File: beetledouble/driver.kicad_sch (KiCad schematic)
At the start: 13 parts, among them J4 motor_out, Q1 IRF8313PBF, Q2 IRF8313PBF, U4 NCP81155MNTXG, U5 NCP81155MNTXG

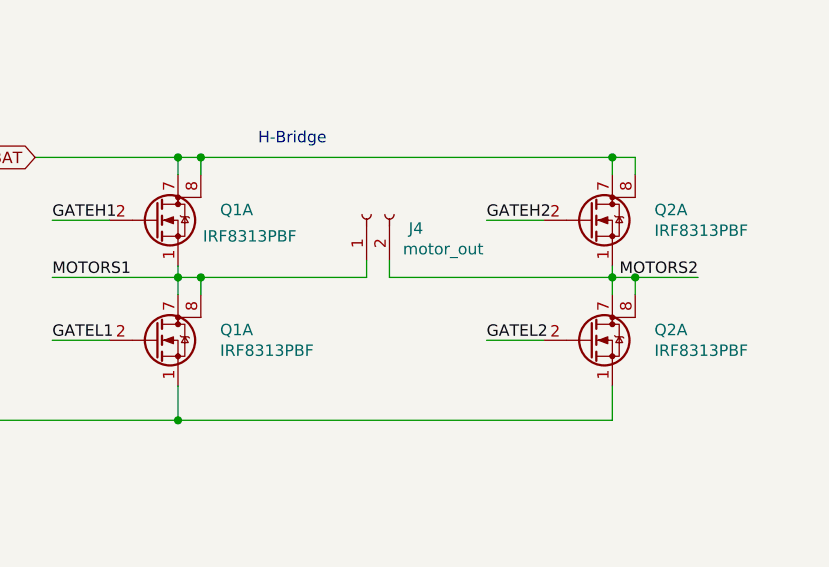
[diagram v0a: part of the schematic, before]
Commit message: Beetle double driver update with differen fets
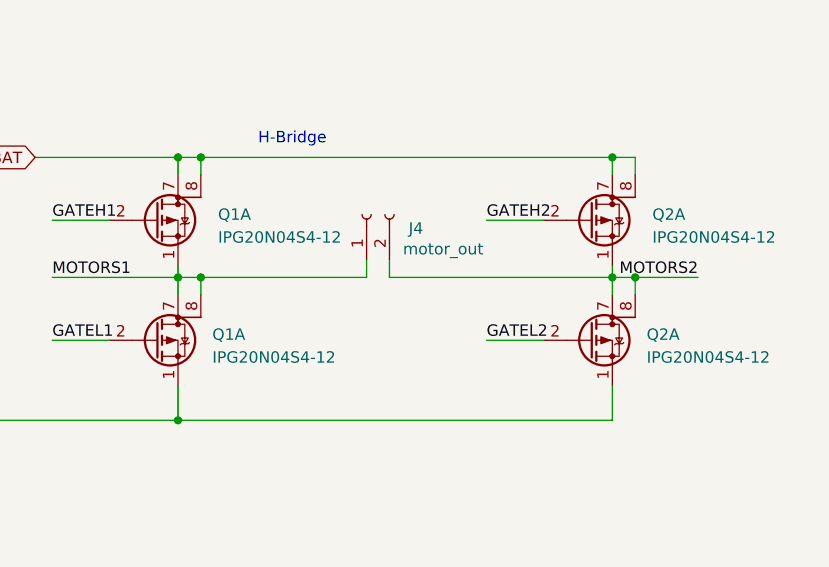
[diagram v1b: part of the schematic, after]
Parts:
- removed Q1 (x2), Q2 (x2): IRF8313PBF, Package_SO:SOIC-8_3.9x4.9mm_P1.27mm, symbol beetletriple:Q_Dual_NMOS_S1G1S2G2D2D2D1D1
- added Q1 (x2), Q2 (x2): IPG20N04S4-12, beetledouble:Infineon-PG-TDSON, symbol Device:Q_Dual_PMOS_S1G1S2G2D2D2D1D1
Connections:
- net GATEH2: now also Q2.2 (G)
- net GATEL2: now also Q2.2 (G)
- net GNDSHUNT: now also Q1.1 (S), Q2.1 (S)
- net MOTORS1: now also Q1.1 (S), Q1.7 (D), Q1.8 (G)
- net MOTORS2: now also Q2.1 (S), Q2.7 (D), Q2.8 (G)
- net TESTH1: now also Q1.2 (G)
- net TESTL1: now also Q1.2 (G)
- net VBAT: now also Q1.7 (D), Q1.8 (G), Q2.7 (D), Q2.8 (G)
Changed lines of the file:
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@@
     (pin "2")
   )
-  (symbol (lib_id "beetletriple:Q_Dual_NMOS_S1G1S2G2D2D2D1D1") (at 201.295 78.74 0)
-    (in_bom yes) (on_board yes)
-    (property "Reference" "Q1" (id 0) (at 208.5087 77.5906 0)
+  (symbol (lib_id "Device:Q_Dual_PMOS_S1G1S2G2D2D2D1D1") (at 201.295 78.74 0)
+    (in_bom yes) (on_board yes) (fields_autoplaced)
+    (property "Reference" "Q1" (id 0) (at 208.28 78.1049 0)
       (effects (font (size 1.27 1.27)) (justify left))
     )
-    (property "Value" "IRF8313PBF " (id 1) (at 206.604 80.524 0)
+    (property "Value" "IPG20N04S4-12" (id 1) (at 208.28 80.6449 0)
       (effects (font (size 1.27 1.27)) (justify left))
     )
-    (property "Footprint" "Package_SO:SOIC-8_3.9x4.9mm_P1.27mm" (id 2) (at 206.375 78.74 0)
+    (property "Footprint" "beetledouble:Infineon-PG-TDSON" (id 2) (at 202.565 78.74 0)
       (effects (font (size 1.27 1.27)) hide)
     )
-    (property "Datasheet" "~" (id 3) (at 206.375 78.74 0)
-      (effects (font (size 1.27 1.27)) hide)
-    )
-    (property "LCSC" "C57696" (id 4) (at 201.295 78.74 0)
+    (property "Datasheet" "~" (id 3) (at 202.565 78.74 0)
       (effects (font (size 1.27 1.27)) hide)
     )
@@
     (pin "8")
   )
-  (symbol (lib_id "beetletriple:Q_Dual_NMOS_S1G1S2G2D2D2D1D1") (at 201.295 92.075 0)
-    (in_bom yes) (on_board yes)
-    (property "Reference" "Q1" (id 0) (at 208.5087 90.9256 0)
+  (symbol (lib_id "Device:Q_Dual_PMOS_S1G1S2G2D2D2D1D1") (at 201.295 92.075 0)
+    (in_bom yes) (on_board yes) (fields_autoplaced)
+    (property "Reference" "Q1" (id 0) (at 207.645 91.4399 0)
       (effects (font (size 1.27 1.27)) (justify left))
     )
-    (property "Value" "IRF8313PBF " (id 1) (at 208.509 93.224 0)
+    (property "Value" "IPG20N04S4-12" (id 1) (at 207.645 93.9799 0)
       (effects (font (size 1.27 1.27)) (justify left))
     )
-    (property "Footprint" "Package_SO:SOIC-8_3.9x4.9mm_P1.27mm" (id 2) (at 206.375 92.075 0)
+    (property "Footprint" "beetledouble:Infineon-PG-TDSON" (id 2) (at 202.565 92.075 0)
       (effects (font (size 1.27 1.27)) hide)
     )
-    (property "Datasheet" "~" (id 3) (at 206.375 92.075 0)
-      (effects (font (size 1.27 1.27)) hide)
-    )
-    (property "LCSC" "C57696" (id 4) (at 201.295 92.075 0)
+    (property "Datasheet" "~" (id 3) (at 202.565 92.075 0)
       (effects (font (size 1.27 1.27)) hide)
     )
@@
     (pin "6")
   )
-  (symbol (lib_id "beetletriple:Q_Dual_NMOS_S1G1S2G2D2D2D1D1") (at 249.555 78.74 0)
-    (in_bom yes) (on_board yes)
-    (property "Reference" "Q2" (id 0) (at 256.7687 77.5906 0)
+  (symbol (lib_id "Device:Q_Dual_PMOS_S1G1S2G2D2D2D1D1") (at 249.555 78.74 0)
+    (in_bom yes) (on_board yes) (fields_autoplaced)
+    (property "Reference" "Q2" (id 0) (at 256.54 78.1049 0)
       (effects (font (size 1.27 1.27)) (justify left))
     )
-    (property "Value" "IRF8313PBF " (id 1) (at 256.769 79.889 0)
+    (property "Value" "IPG20N04S4-12" (id 1) (at 256.54 80.6449 0)
       (effects (font (size 1.27 1.27)) (justify left))
     )
-    (property "Footprint" "Package_SO:SOIC-8_3.9x4.9mm_P1.27mm" (id 2) (at 254.635 78.74 0)
+    (property "Footprint" "beetledouble:Infineon-PG-TDSON" (id 2) (at 250.825 78.74 0)
       (effects (font (size 1.27 1.27)) hide)
     )
-    (property "Datasheet" "~" (id 3) (at 254.635 78.74 0)
-      (effects (font (size 1.27 1.27)) hide)
-    )
-    (property "LCSC" "C57696" (id 4) (at 249.555 78.74 0)
+    (property "Datasheet" "~" (id 3) (at 250.825 78.74 0)
       (effects (font (size 1.27 1.27)) hide)
     )
@@
     (pin "8")
   )
-  (symbol (lib_id "beetletriple:Q_Dual_NMOS_S1G1S2G2D2D2D1D1") (at 249.555 92.075 0)
-    (in_bom yes) (on_board yes)
-    (property "Reference" "Q2" (id 0) (at 256.7687 90.9256 0)
+  (symbol (lib_id "Device:Q_Dual_PMOS_S1G1S2G2D2D2D1D1") (at 249.555 92.075 0)
+    (in_bom yes) (on_board yes) (fields_autoplaced)
+    (property "Reference" "Q2" (id 0) (at 255.905 91.4399 0)
       (effects (font (size 1.27 1.27)) (justify left))
     )
-    (property "Value" "IRF8313PBF " (id 1) (at 256.769 93.224 0)
+    (property "Value" "IPG20N04S4-12" (id 1) (at 255.905 93.9799 0)
       (effects (font (size 1.27 1.27)) (justify left))
     )
-    (property "Footprint" "Package_SO:SOIC-8_3.9x4.9mm_P1.27mm" (id 2) (at 254.635 92.075 0)
+    (property "Footprint" "beetledouble:Infineon-PG-TDSON" (id 2) (at 250.825 92.075 0)
       (effects (font (size 1.27 1.27)) hide)
     )
-    (property "Datasheet" "~" (id 3) (at 254.635 92.075 0)
+    (property "Datasheet" "~" (id 3) (at 250.825 92.075 0)
       (effects (font (size 1.27 1.27)) hide)
     )
-    (property "LCSC" "C57696" (id 4) (at 249.555 92.075 0)
-      (effects (font (size 1.27 1.27)) hide)
-    )

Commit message: beetledouble esc wip
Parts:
- renumbered C3 to C5, C4 to C6, J4 to J5, Q1 to Q3, Q2 to Q4, R1 to R5, R2 to R6, R3 to R7, R4 to R8, U4 to U6, U5 to U7
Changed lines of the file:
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@@
   (symbol (lib_id "power:+12V") (at 48.26 91.44 0)
     (in_bom yes) (on_board yes)
-    (property "Reference" "#PWR06" (id 0) (at 48.26 95.25 0)
+    (property "Reference" "#PWR010" (id 0) (at 48.26 95.25 0)
       (effects (font (size 1.27 1.27)) hide)
     )
@@
   (symbol (lib_id "power:+12V") (at 48.895 40.64 0)
     (in_bom yes) (on_board yes)
-    (property "Reference" "#PWR08" (id 0) (at 48.895 44.45 0)
+    (property "Reference" "#PWR012" (id 0) (at 48.895 44.45 0)
       (effects (font (size 1.27 1.27)) hide)
     )
@@
   (symbol (lib_id "power:GND") (at 48.26 115.57 0)
     (in_bom yes) (on_board yes)
-    (property "Reference" "#PWR07" (id 0) (at 48.26 121.92 0)
+    (property "Reference" "#PWR011" (id 0) (at 48.26 121.92 0)
       (effects (font (size 1.27 1.27)) hide)
     )
@@
   (symbol (lib_id "power:GND") (at 48.895 64.77 0)
     (in_bom yes) (on_board yes)
-    (property "Reference" "#PWR09" (id 0) (at 48.895 71.12 0)
+    (property "Reference" "#PWR013" (id 0) (at 48.895 71.12 0)
       (effects (font (size 1.27 1.27)) hide)
     )
@@
   (symbol (lib_id "Device:R") (at 75.565 101.6 90)
     (in_bom yes) (on_board yes)
-    (property "Reference" "R1" (id 0) (at 75.565 96.3738 90))
+    (property "Reference" "R5" (id 0) (at 75.565 96.3738 90))
     (property "Value" "10R" (id 1) (at 75.565 98.6725 90))
     (property "Footprint" "Resistor_SMD:R_0603_1608Metric" (id 2) (at 75.565 103.378 90)
@@
   (symbol (lib_id "Device:R") (at 75.565 109.22 90)
     (in_bom yes) (on_board yes)
-    (property "Reference" "R2" (id 0) (at 75.565 103.9938 90))
+    (property "Reference" "R6" (id 0) (at 75.565 103.9938 90))
     (property "Value" "10R" (id 1) (at 75.565 106.2925 90))
     (property "Footprint" "Resistor_SMD:R_0603_1608Metric" (id 2) (at 75.565 110.998 90)
@@
   (symbol (lib_id "Device:R") (at 79.375 50.8 90)
     (in_bom yes) (on_board yes)
-    (property "Reference" "R3" (id 0) (at 79.375 45.5738 90))
+    (property "Reference" "R7" (id 0) (at 79.375 45.5738 90))
     (property "Value" "10R" (id 1) (at 79.375 47.8725 90))
     (property "Footprint" "Resistor_SMD:R_0603_1608Metric" (id 2) (at 79.375 52.578 90)
@@
   (symbol (lib_id "Device:R") (at 79.375 58.42 90)
     (in_bom yes) (on_board yes)
-    (property "Reference" "R4" (id 0) (at 79.375 53.1938 90))
+    (property "Reference" "R8" (id 0) (at 79.375 53.1938 90))
     (property "Value" "10R" (id 1) (at 79.375 55.4925 90))
     (property "Footprint" "Resistor_SMD:R_0603_1608Metric" (id 2) (at 79.375 60.198 90)
@@
   (symbol (lib_id "Connector:Conn_01x02_Female") (at 224.79 78.105 90)
     (in_bom yes) (on_board yes)
-    (property "Reference" "J4" (id 0) (at 229.4637 79.648 90)
+    (property "Reference" "J5" (id 0) (at 229.4637 79.648 90)
       (effects (font (size 1.27 1.27)) (justify right))
     )
@@
   (symbol (lib_id "Device:C") (at 69.215 92.71 0)
     (in_bom yes) (on_board yes)
-    (property "Reference" "C3" (id 0) (at 72.136 91.561 0)
+    (property "Reference" "C5" (id 0) (at 72.136 91.561 0)
       (effects (font (size 1.27 1.27)) (justify left))
     )
@@
   (symbol (lib_id "Device:C") (at 69.85 41.91 0)
     (in_bom yes) (on_board yes)
-    (property "Reference" "C4" (id 0) (at 72.7711 40.7606 0)
+    (property "Reference" "C6" (id 0) (at 72.7711 40.7606 0)
       (effects (font (size 1.27 1.27)) (justify left))
     )
@@
   (symbol (lib_id "Device:Q_Dual_PMOS_S1G1S2G2D2D2D1D1") (at 201.295 78.74 0)
     (in_bom yes) (on_board yes) (fields_autoplaced)
-    (property "Reference" "Q1" (id 0) (at 208.28 78.1049 0)
+    (property "Reference" "Q3" (id 0) (at 208.28 78.1049 0)
       (effects (font (size 1.27 1.27)) (justify left))
     )
@@
   (symbol (lib_id "Device:Q_Dual_PMOS_S1G1S2G2D2D2D1D1") (at 201.295 92.075 0)
     (in_bom yes) (on_board yes) (fields_autoplaced)
-    (property "Reference" "Q1" (id 0) (at 207.645 91.4399 0)
+    (property "Reference" "Q3" (id 0) (at 207.645 91.4399 0)
       (effects (font (size 1.27 1.27)) (justify left))
     )
@@
   (symbol (lib_id "Device:Q_Dual_PMOS_S1G1S2G2D2D2D1D1") (at 249.555 78.74 0)
     (in_bom yes) (on_board yes) (fields_autoplaced)
-    (property "Reference" "Q2" (id 0) (at 256.54 78.1049 0)
+    (property "Reference" "Q4" (id 0) (at 256.54 78.1049 0)
       (effects (font (size 1.27 1.27)) (justify left))
     )
@@
   (symbol (lib_id "Device:Q_Dual_PMOS_S1G1S2G2D2D2D1D1") (at 249.555 92.075 0)
     (in_bom yes) (on_board yes) (fields_autoplaced)
-    (property "Reference" "Q2" (id 0) (at 255.905 91.4399 0)
+    (property "Reference" "Q4" (id 0) (at 255.905 91.4399 0)
       (effects (font (size 1.27 1.27)) (justify left))
     )
@@
   (symbol (lib_id "beetledouble:NCP81155MN") (at 48.26 105.41 0)
     (in_bom yes) (on_board yes)
-    (property "Reference" "U4" (id 0) (at 50.483 89.516 0))
+    (property "Reference" "U6" (id 0) (at 50.483 89.516 0))
     (property "Value" "NCP81155MNTXG" (id 1) (at 56.8325 91.8145 0))
     (property "Footprint" "beetledouble:DFN-8-3x3mm_hand1" (id 2) (at 48.26 105.41 0)
@@
   (symbol (lib_id "beetledouble:NCP81155MN") (at 48.895 54.61 0)
     (in_bom yes) (on_board yes)
-    (property "Reference" "U5" (id 0) (at 51.117 38.716 0))
+    (property "Reference" "U7" (id 0) (at 51.117 38.716 0))
     (property "Value" "NCP81155MNTXG" (id 1) (at 57.4675 41.0145 0))
     (property "Footprint" "beetledouble:DFN-8-3x3mm_hand1" (id 2) (at 48.895 54.61 0)

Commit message: Beetle esc
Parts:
- removed U6, U7: NCP81155MNTXG, beetledouble:DFN-8-3x3mm_hand1, symbol beetledouble:NCP81155MN
- added D5, D6: B5819W, Diode_SMD:D_SOD-123, symbol Device:D_Schottky
- added U6, U7: ADP3110A, beetledouble:DFN-8-3x3mm_hand1, symbol beetledouble:ADP3110A
- Q3, Q4: value IPG20N04S4-12 -> AON6884; LCSC (none) -> C125872
- R5, R6, R7, R8: LCSC (none) -> C22859
- renumbered C6 to C5, C5 to C6
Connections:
- net +12V: now also D5.2 (A), D6.2 (A), U6.4 (VCC), U7.4 (VCC)
- net GND: now also U6.6 (GND), U6.9 (PAD), U7.6 (GND), U7.9 (PAD)
- net MOTORD1: now also U6.2 (IN)
- net MOTORD2: now also U7.2 (IN)
- net MOTOREN: now also U6.3 (~OD), U7.3 (~OD)
- net MOTORH1: now also U6.8 (DRVH)
- net MOTORH2: now also U7.8 (DRVH)
- net MOTORL1: now also U6.5 (DRVL)
- net MOTORL2: now also U7.5 (DRVL)
- net MOTORS1: now also U6.7 (SW)
- net MOTORS2: now also U7.7 (SW)
- net BOOST1: now reaches C5.1
- net BOOST1: now also D5.1 (K), U6.1 (BST)
- net BOOST2: now reaches C6.1
- net BOOST2: now also D6.1 (K), U7.1 (BST)
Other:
- moved on the sheet: C5, C6, R5, R6, R7, R8

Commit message: Beetledouble ESC
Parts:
- added C14, C15: 10uF 50V, Capacitor_SMD:C_1206_3216Metric, symbol Device:C
- added C16, C18: DNP, Capacitor_SMD:C_1206_3216Metric, symbol Device:C
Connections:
- net GNDSHUNT: now also C14.2, C15.2, C16.2, C18.2
- net VBAT: now also C14.1, C15.1, C16.1, C18.1
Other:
- moved on the sheet: J5, Q3A, Q4A

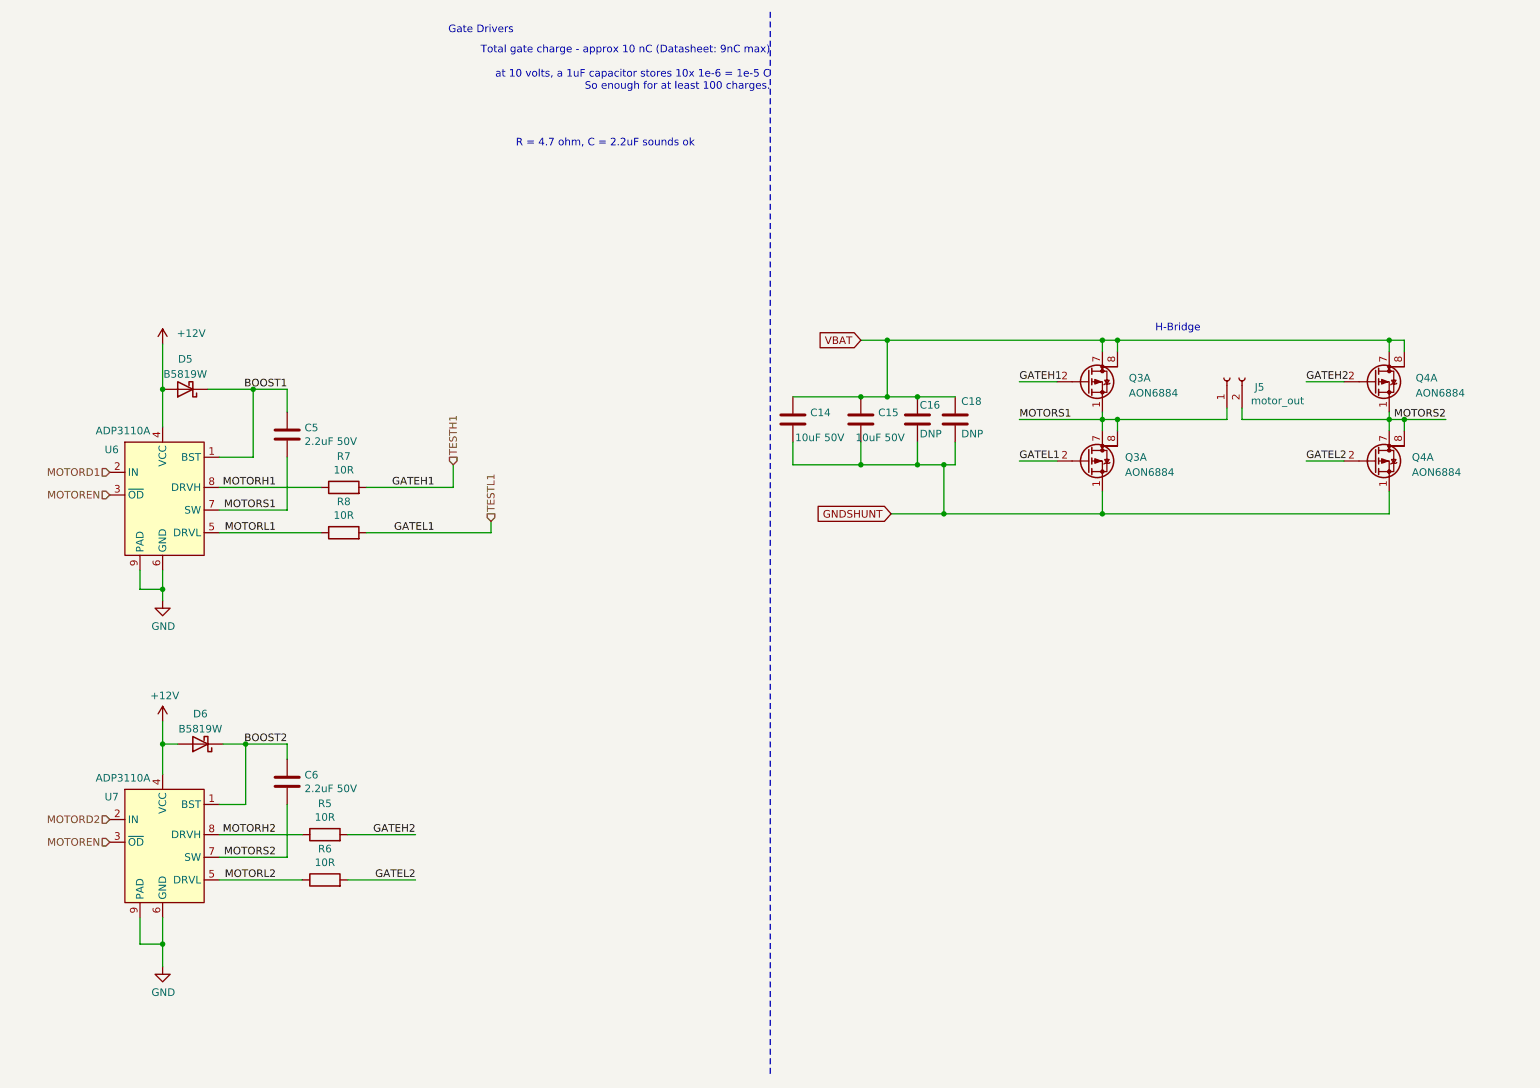
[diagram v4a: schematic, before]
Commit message: fix capcitor lcsc id, change driver chip to NCP81155
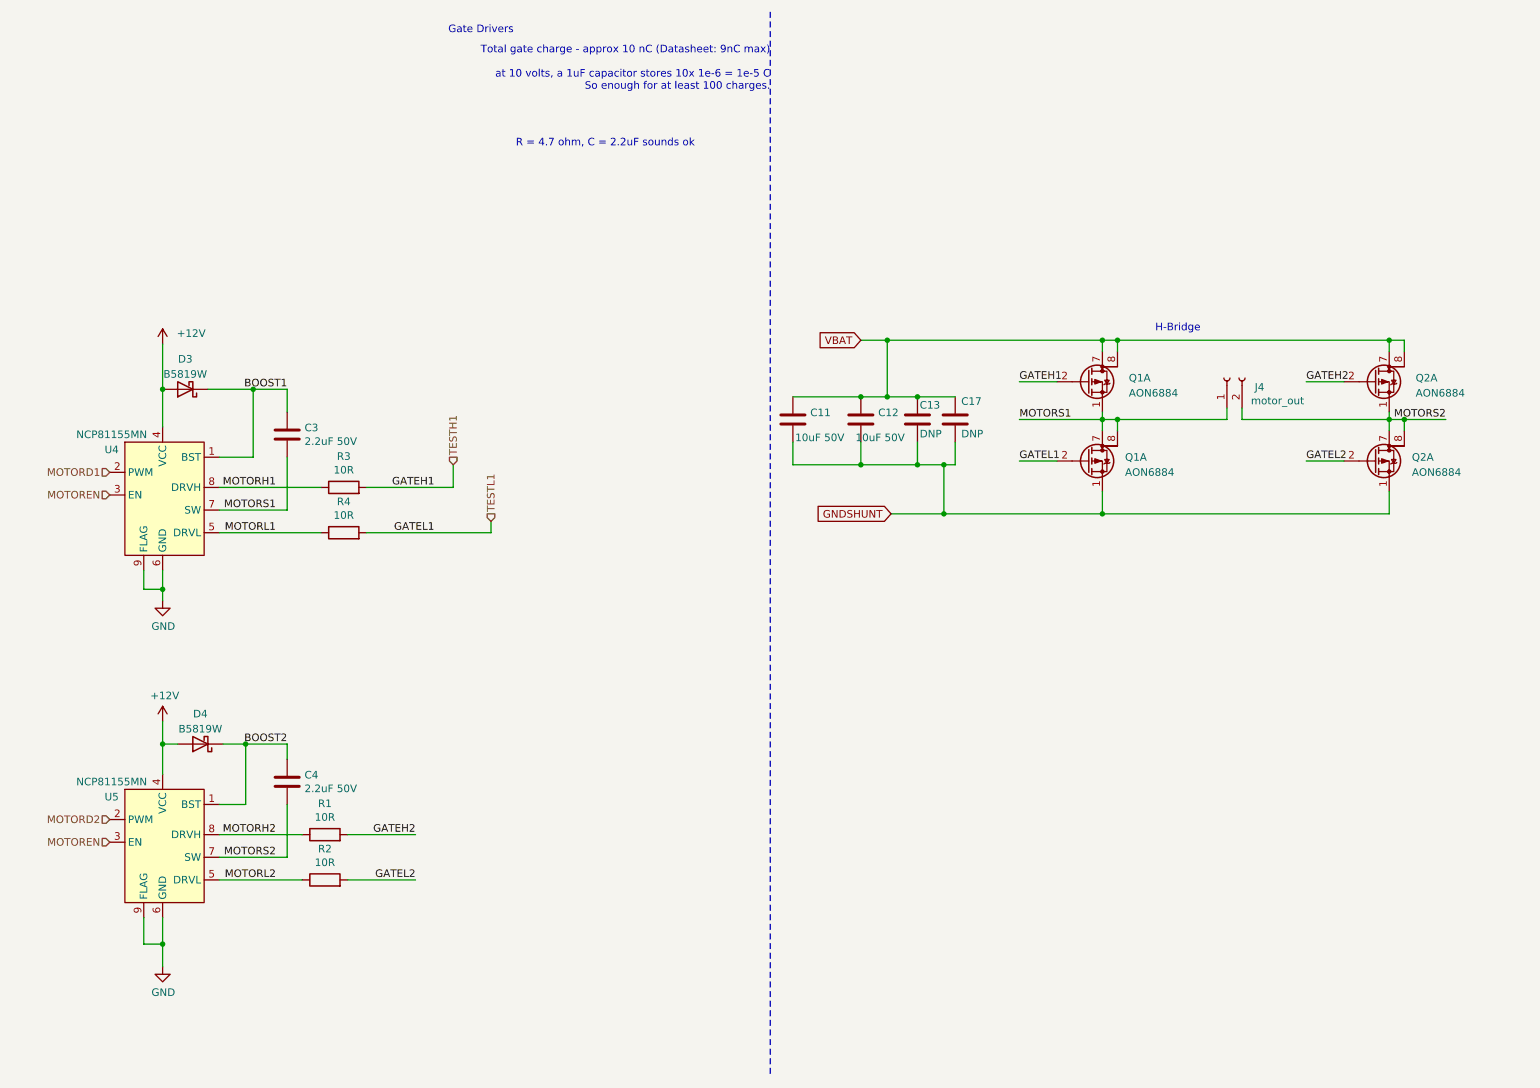
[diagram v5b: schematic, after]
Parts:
- removed U6, U7: ADP3110A, beetledouble:DFN-8-3x3mm_hand1, symbol beetledouble:ADP3110A
- added U4, U5: NCP81155MN, beetledouble:DFN-8-3x3mm_hand1, symbol beetledouble:NCP81155MN
- C3: renamed from C5; LCSC C50254 -> C326557
- C4: renamed from C6; LCSC C50254 -> C326557
- renumbered C14 to C11, C15 to C12, C16 to C13, C18 to C17, D5 to D3, D6 to D4, J5 to J4, Q3 to Q1, Q4 to Q2, R5 to R1, R6 to R2, R7 to R3, R8 to R4
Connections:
- net +12V: now also U4.4 (VCC), U5.4 (VCC)
- net BOOST1: now also U4.1 (BST)
- net BOOST2: now also U5.1 (BST)
- net GND: now also U4.6 (GND), U4.9 (FLAG), U5.6 (GND), U5.9 (FLAG)
- net MOTORD1: now also U4.2 (PWM)
- net MOTORD2: now also U5.2 (PWM)
- net MOTOREN: now also U4.3 (EN), U5.3 (EN)
- net MOTORH1: now also U4.8 (DRVH)
- net MOTORH2: now also U5.8 (DRVH)
- net MOTORL1: now also U4.5 (DRVL)
- net MOTORL2: now also U5.5 (DRVL)
- net MOTORS1: now also U4.7 (SW)
- net MOTORS2: now also U5.7 (SW)
